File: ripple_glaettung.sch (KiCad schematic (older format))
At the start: 8 parts, among them J1 Screw_Terminal_01x02, J2 Screw_Terminal_01x02, Q1 TIP3055

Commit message: minor change
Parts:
- added HS1: Heatsink, symbol Mechanical:Heatsink
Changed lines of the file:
@@
 	0    -1   -1   0
 $EndComp
+$Comp
+L Mechanical:Heatsink HS1
+U 1 1 5F2ADEAD
+P 6150 2400
+F 0 "HS1" H 6292 2521 50  0000 L CNN
+F 1 "Heatsink" H 6292 2430 50  0000 L CNN
+F 2 "" H 6162 2400 50  0001 C CNN
+F 3 "~" H 6162 2400 50  0001 C CNN
+	1    6150 2400
+	1    0    0    -1
+$EndComp
 $EndSCHEMATC

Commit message: fine tuning pcb picture
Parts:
- HS1: footprint (none) -> Heatsink:Heatsink_Fischer_SK129-STS_42x25mm_2xDrill2.5mm
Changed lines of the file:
@@
 $EndComp
 $Comp
-L power:GND #PWR0101
+L power:GND #PWR02
 U 1 1 5EE53753
 P 3650 4800
-F 0 "#PWR0101" H 3650 4550 50  0001 C CNN
+F 0 "#PWR02" H 3650 4550 50  0001 C CNN
 F 1 "GND" H 3655 4627 50  0000 C CNN
 F 2 "" H 3650 4800 50  0001 C CNN
@@
 $EndComp
 $Comp
-L power:VCC #PWR0102
+L power:VCC #PWR01
 U 1 1 5EE53F53
 P 3650 2950
-F 0 "#PWR0102" H 3650 2800 50  0001 C CNN
+F 0 "#PWR01" H 3650 2800 50  0001 C CNN
 F 1 "VCC" H 3665 3123 50  0000 C CNN
 F 2 "" H 3650 2950 50  0001 C CNN
@@
 F 0 "HS1" H 6292 2521 50  0000 L CNN
 F 1 "Heatsink" H 6292 2430 50  0000 L CNN
-F 2 "" H 6162 2400 50  0001 C CNN
+F 2 "Heatsink:Heatsink_Fischer_SK129-STS_42x25mm_2xDrill2.5mm" H 6162 2400 50  0001 C CNN
 F 3 "~" H 6162 2400 50  0001 C CNN
 	1    6150 2400

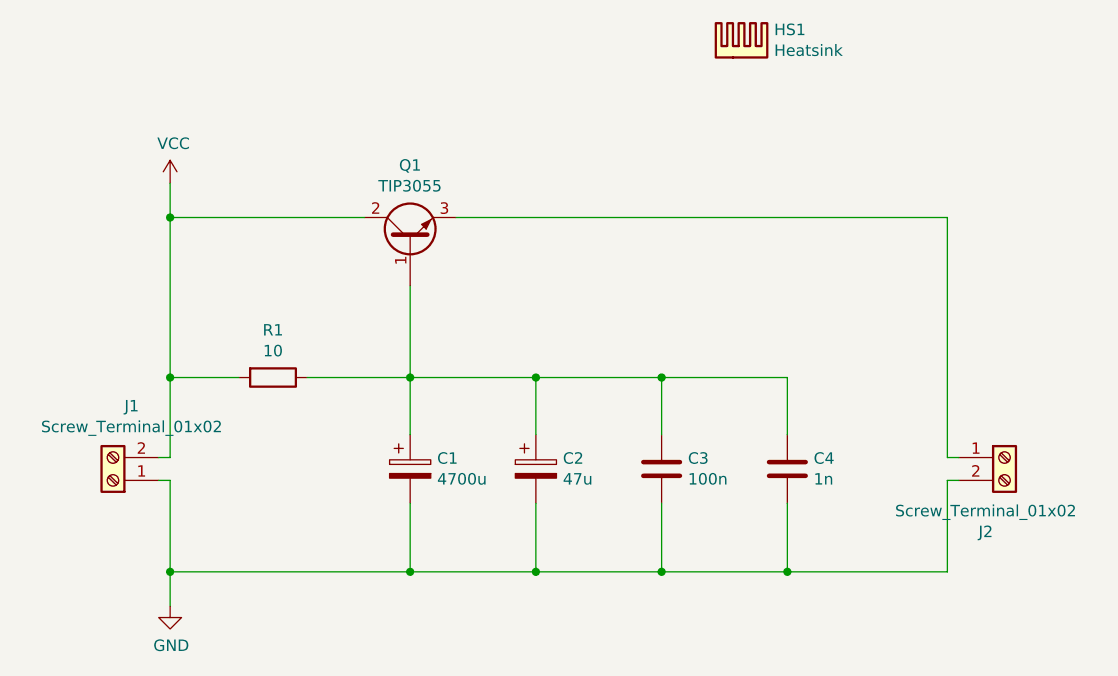
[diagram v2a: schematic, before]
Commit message: added recommendation for TIP142 Darlington
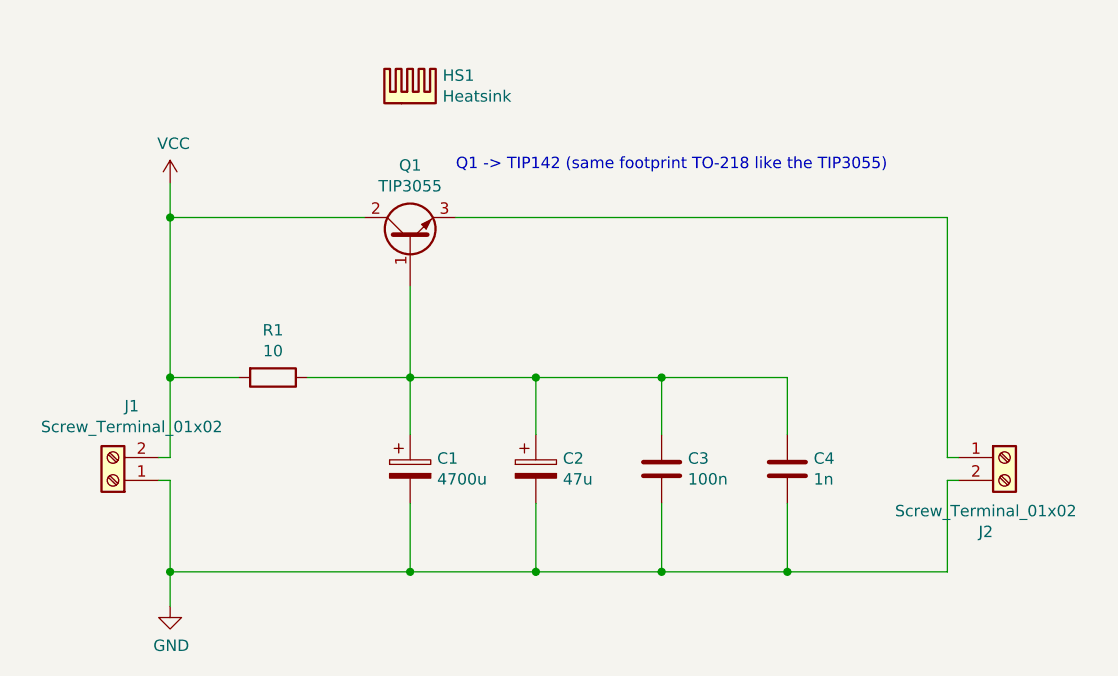
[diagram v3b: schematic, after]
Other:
- note added: "Q1 -> TIP142 (same footprint TO-218 like the TIP3055)"
- moved on the sheet: HS1
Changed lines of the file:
@@
 L Mechanical:Heatsink HS1
 U 1 1 5F2ADEAD
-P 6150 2400
-F 0 "HS1" H 6292 2521 50  0000 L CNN
-F 1 "Heatsink" H 6292 2430 50  0000 L CNN
-F 2 "Heatsink:Heatsink_Fischer_SK129-STS_42x25mm_2xDrill2.5mm" H 6162 2400 50  0001 C CNN
-F 3 "~" H 6162 2400 50  0001 C CNN
-	1    6150 2400
+P 4700 2600
+F 0 "HS1" H 4842 2721 50  0000 L CNN
+F 1 "Heatsink" H 4842 2630 50  0000 L CNN
+F 2 "Heatsink:Heatsink_Fischer_SK129-STS_42x25mm_2xDrill2.5mm" H 4712 2600 50  0001 C CNN
+F 3 "~" H 4712 2600 50  0001 C CNN
+	1    4700 2600
 	1    0    0    -1
 $EndComp
+Text Notes 4900 2900 0    50   ~ 0
+Q1 -> TIP142 (same footprint TO-218 like the TIP3055)
 $EndSCHEMATC
